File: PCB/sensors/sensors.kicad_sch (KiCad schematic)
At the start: 16 parts, among them J1 Conn_01x07_Socket, U1 BME680

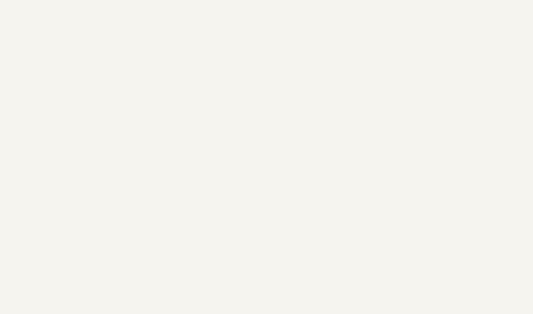
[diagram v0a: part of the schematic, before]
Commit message: Added setup, read and get Command
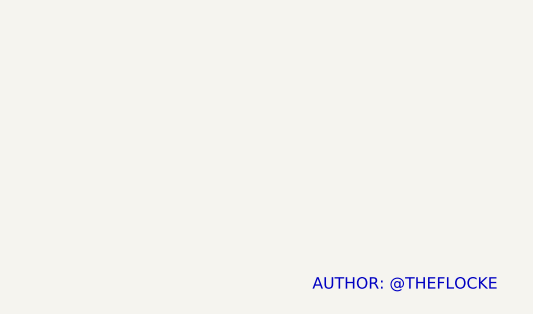
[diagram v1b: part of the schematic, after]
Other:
- note added: "AUTHOR: @THEFLOCKE"
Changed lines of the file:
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@@
 	(generator_version "9.0")
 	(paper "A4")
+	(text "AUTHOR: @THEFLOCKE"
+		(exclude_from_sim no)
+		(at 249.936 196.596 0)
+		(effects
+			(font
+				(face "KiCad Font")
+				(size 1.27 1.27)
+				(color 194 0 194 1)
+			)
+		)
+	)
 	(junction
 		(at 99.06 74.93)
